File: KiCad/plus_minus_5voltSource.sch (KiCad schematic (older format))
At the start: 16 parts, among them J1 USB_OTG, P1 CONN_01X03, SW1 SW_Push, U1 LM7805, U2 7660, U3 MC79L05A

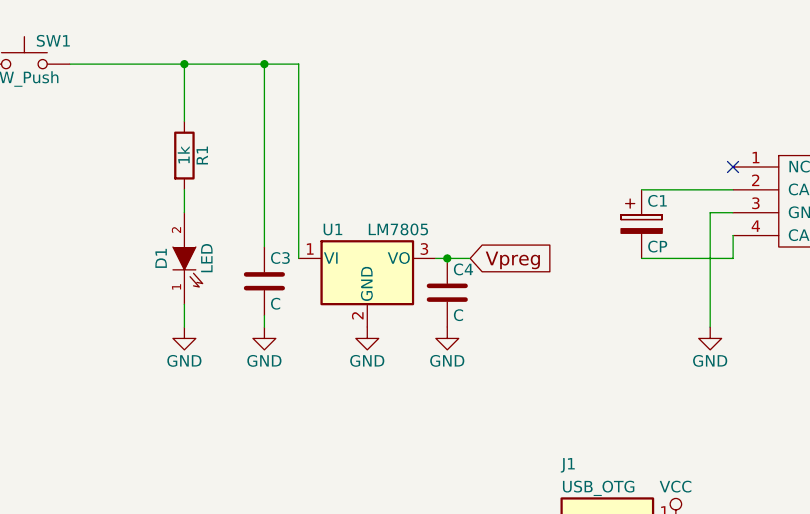
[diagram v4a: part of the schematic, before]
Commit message: Changed schematic to reflect correct +5V regulator part number. Saved new PDF schematic sheet. Edited bom to have correct regulator digikey part number.
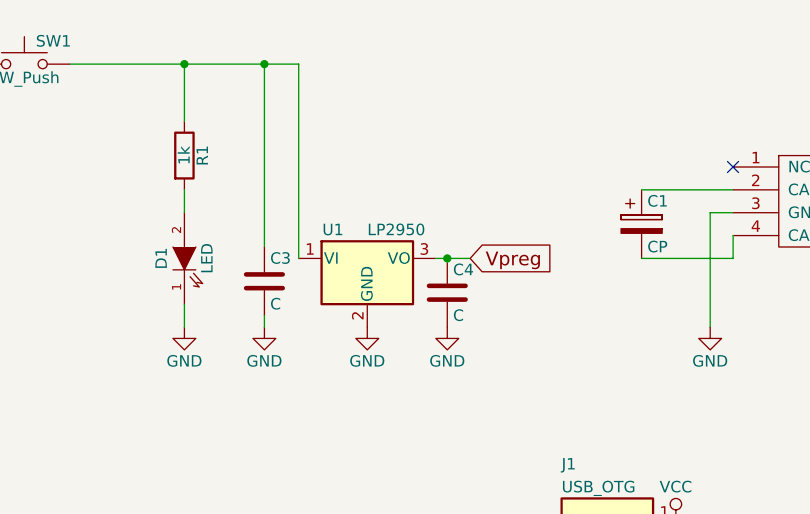
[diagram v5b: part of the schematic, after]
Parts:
- U1: value LM7805 -> LP2950
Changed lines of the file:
@@
 P 3950 3550
 F 0 "U1" H 3800 3675 50  0000 C CNN
-F 1 "LM7805" H 3950 3675 50  0000 L CNN
+F 1 "LP2950" H 3950 3675 50  0000 L CNN
 F 2 "TO_SOT_Packages_THT:TO-92_Inline_Narrow_Oval" H 3950 3775 50  0001 C CIN
 F 3 "" H 3950 3500 50  0001 C CNN
